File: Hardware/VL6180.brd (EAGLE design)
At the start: 44.5 x 13 mm, 24 parts, among them U1 VL6180, U3 MIC5219 3.3V

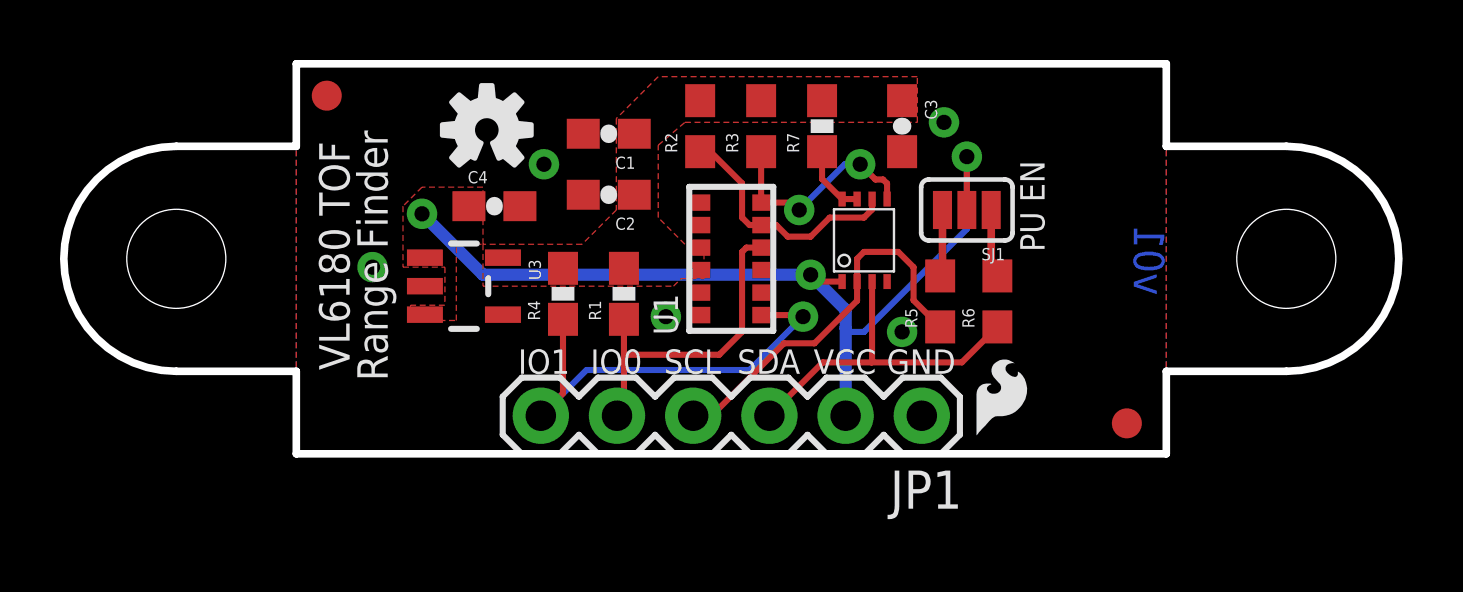
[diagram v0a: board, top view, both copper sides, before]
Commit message: fixed flipped pin problem.  8-9 on the sensor were reversed somehow.  All better :)
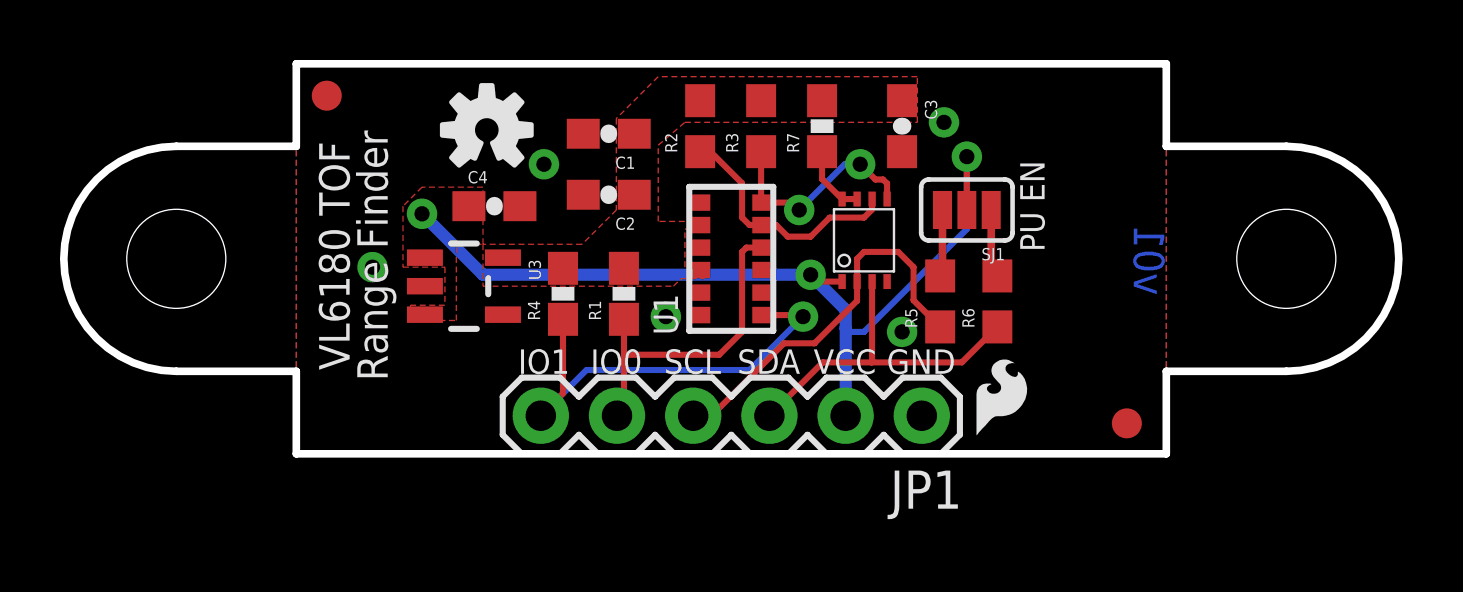
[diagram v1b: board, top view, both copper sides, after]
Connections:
- net 2.8V: now also U1.8; no longer U1.9
- net GND: now also U1.9; no longer U1.8
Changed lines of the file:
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@@
 </signal>
 <signal name="GND">
-<contactref element="U1" pad="8"/>
+<contactref element="U1" pad="9"/>
 <contactref element="U1" pad="12"/>
 <contactref element="C2" pad="2"/>
@@
 <contactref element="C2" pad="1"/>
 <contactref element="C1" pad="1"/>
-<contactref element="U1" pad="9"/>
+<contactref element="U1" pad="8"/>
 <contactref element="U1" pad="10"/>
 <contactref element="R4" pad="2"/>
@@
 <vertex x="12.827" y="5.842"/>
 <vertex x="13.589" y="5.842"/>
-<vertex x="13.589" y="6.985"/>
-<vertex x="12.954" y="6.985"/>
-<vertex x="12.065" y="7.874"/>
+<vertex x="13.589" y="6.223"/>
+<vertex x="12.954" y="6.223"/>
+<vertex x="12.954" y="7.493"/>
+<vertex x="13.589" y="7.493"/>
+<vertex x="13.589" y="7.747"/>
+<vertex x="12.065" y="7.747"/>
 <vertex x="12.065" y="10.287"/>
 <vertex x="12.954" y="11.049"/>

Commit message: added pin 1 designator
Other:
- board text added: "v02"
- board text removed: "v01"
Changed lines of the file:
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@@
 <wire x1="-3.99974375" y1="2.750590625" x2="-3.99974375" y2="10.250590625" width="0.254" layer="20" curve="-180"/>
 <wire x1="33.00025625" y1="10.250590625" x2="33.00025625" y2="2.750590625" width="0.254" layer="20" curve="-180"/>
-<text x="28.932" y="6.454" size="1.016" layer="16" font="vector" ratio="20" rot="MR270" align="bottom-center">v01</text>
+<text x="28.932" y="6.454" size="1.016" layer="16" font="vector" ratio="20" rot="MR270" align="bottom-center">v02</text>
 <text x="20.828" y="2.667" size="0.8128" layer="21" font="vector" ratio="15" align="bottom-center">GND</text>
 <text x="18.288" y="2.667" size="0.8128" layer="21" font="vector" ratio="15" align="bottom-center">VCC</text>
